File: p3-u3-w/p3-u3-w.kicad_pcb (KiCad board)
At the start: 2 copper layers, 14 x 90 mm, 104 parts, among them J1 SWD_pin, J2 Display, J3 SJ-3524-SMT, J4 473092651, J5 UART, J6 12401826E412A, J7 Bat Conn, J8 CONMHF1-SMD-G-T, SW1 SW_SPST, SW2 SW_SPST, SW3 SW_SPST, SW4 SW_SPST, SW5 SW_SPST, SW6 SW_SPST, SW7 SW_SPST, U1 LSM6DSM, U2 PCM5102A, U3 STM32WB55CEUx, U4 LD39050PU33R, U5 TPS63802DLAR, U6 MCP73831T-2ACI/OT, U7 DLF162500LT-5028A1, X1 NX2016SA-32MHZ-EXS00A-CS06654, Y2 32k768

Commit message: changed some routing
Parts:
- C1, C10, C11, C12, C15, C16, C17, C18, C19, C2, C20, C21, C22, C23, C24, C25, C26, C27, C28, C29, C3, C30, C31, C32, C33, C34, C35, C36, C37, C38, C39, C4, C40, C41, C42, C5, C6, C7, C8, C9: footprint Capacitor_SMD:C_0603_1608Metric -> Capacitor_SMD:C_0402_1005Metric
- C13, C14: footprint Capacitor_SMD:C_0603_1608Metric -> Capacitor_SMD:C_0402_1005Metric; moved to B.Cu
- L1: moved to B.Cu
- R1, R17, R18, R19, R2, R20, R21, R3, R4: footprint Resistor_SMD:R_0603_1608Metric -> Resistor_SMD:R_0402_1005Metric; moved to B.Cu
- R10, R11, R12, R13, R14, R15, R16, R22, R23, R24, R25, R26, R27, R28, R29, R30, R5, R6, R7, R8, R9: footprint Resistor_SMD:R_0603_1608Metric -> Resistor_SMD:R_0402_1005Metric
- moved R3 89.5 mm to (149.0, 78.2)
- moved R4 87.4 mm to (146.6, 78.2), turned to 180 degrees
- moved L1 82.9 mm to (145.5, 108.4), turned to 180 degrees
- moved R2 73.3 mm to (152.8, 56.9)
- moved R20 72.1 mm to (152.7, 70.1)
- moved R21 70.0 mm to (152.7, 79.5)
- moved R19 67.5 mm to (142.5, 56.9), turned to 180 degrees
- moved C13 64.0 mm to (148.7, 83.7), turned to 90 degrees
- moved C14 61.2 mm to (146.1, 83.7), turned to 90 degrees
- moved R1 60.8 mm to (145.8, 79.2)
- moved R18 60.7 mm to (142.5, 70.1), turned to 180 degrees
- moved R17 58.1 mm to (142.6, 79.5), turned to 180 degrees
- moved SW2 26.8 mm to (149.8, 111.7), turned to -90 degrees
- moved C15 11.8 mm to (153.4, 120.2), turned to 0 degrees
- moved U7 9.21 mm to (70.2, 100.3)
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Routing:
- net USB_VBUS: track 49.4 -> 33.2 mm, vias 4 -> 2
- net GND: track 48.0 -> 59.8 mm, vias 27 -> 36
- net +3V3: track 51.4 -> 60.7 mm, vias 10 -> 23
- net /MCU/SWCLK: track 8.54 -> 1.24 mm, vias 0 -> 1
- net Net-(J6-CC1): track 11.1 -> 4.98 mm, vias 2 -> 0
- net /USB_PWR/BAT+: track 18.4 -> 14.3 mm
- net /MCU/SWDIO: track 5.44 -> 1.60 mm, vias 0 -> 1
- net USB_D+: track 8.59 -> 12.0 mm
- net USB_D-: track 13.9 -> 17.0 mm, vias 3 -> 4
- net Net-(U3-PC15): track 4.91 -> 2.88 mm
- net Net-(U5-L1): track 0.00 -> 1.93 mm
- net Net-(U5-L2): track 0.00 -> 1.69 mm
- net Net-(U5-PG): track 4.06 -> 2.39 mm
- net Net-(U5-FB): track 5.43 -> 3.91 mm
- net /MCU/RF1: track 1.02 -> 2.51 mm
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- added copper zone on In1.Cu, net GND
- added copper zone on In4.Cu, net GND
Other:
- copper layers 2 -> 6

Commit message: added in some more routing.
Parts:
- C30, C31: moved to B.Cu
- moved C31 102.2 mm to (153.8, 93.9), turned to 90 degrees
- moved C24 102.1 mm to (149.9, 84.1), turned to 180 degrees
- moved C17 101.9 mm to (149.3, 73.7), turned to 180 degrees
- moved C30 101.7 mm to (153.0, 88.3)
- moved C29 100.8 mm to (146.5, 108.7), turned to 90 degrees
- moved C25 100.3 mm to (149.9, 85.3), turned to 180 degrees
- moved R12 99.8 mm to (152.0, 100.9)
- moved R13 98.8 mm to (151.9, 99.6), turned to 180 degrees
- moved C32 97.6 mm to (153.3, 92.2)
- moved R7 96.5 mm to (148.3, 84.9), turned to 90 degrees
- moved R6 95.2 mm to (146.9, 73.5), turned to 90 degrees
- moved R15 95.1 mm to (151.6, 116.2), turned to 180 degrees
- moved R26 94.6 mm to (151.3, 119.0), turned to -90 degrees
- moved R5 94.0 mm to (145.8, 73.5), turned to 90 degrees
- moved R16 94.0 mm to (153.8, 90.8), turned to -90 degrees
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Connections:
- C1 pad 2: +3V3 -> +3.3V
- C10 pad 2: +3V3 -> +3.3V
- C11 pad 2: +3V3 -> +3.3V
- C12 pad 2: +3V3 -> +3.3V
- C13 pad 2: +3V3 -> +3.3V
- C14 pad 2: +3V3 -> +3.3V
- C18 pad 1: GND -> GNDA
- C18 pad 2: +3.3V -> +3.3VA
- C19 pad 2: GND -> GNDA
- C2 pad 2: +3V3 -> +3.3V
- C20 pad 1: GND -> GNDA
- C20 pad 2: +3.3V -> +3.3VA
- C21 pad 2: GND -> GNDA
- C22 pad 1: GND -> GNDA
- C22 pad 2: +3.3V -> +3.3VA
- C23 pad 1: GND -> GNDA
- C23 pad 2: +3.3V -> +3.3VA
- C24 pad 1: GND -> GNDA
- C25 pad 1: GND -> GNDA
- C26 pad 2: GND -> GNDA
- C27 pad 1: GND -> GNDA
- C27 pad 2: +3.3V -> +3.3VA
- C28 pad 1: GND -> GNDA
- C28 pad 2: +3.3V -> +3.3VA
- C3 pad 2: +3V3 -> +3.3V
- C35 pad 1: +3V3 -> +3.3V
- C36 pad 1: +3V3 -> +3.3V
- C4 pad 2: +3V3 -> +3.3V
- C40 pad 1: +3V3 -> +3.3V
- C5 pad 2: +3V3 -> +3.3V
- C6 pad 2: +3V3 -> +3.3V
- C7 pad 2: +3V3 -> +3.3V
- C8 pad 2: +3V3 -> +3.3V
- C9 pad 2: +3V3 -> +3.3V
- J1 pad 2: +3V3 -> +3.3V
- J2 pad 2: +3V3 -> +3.3V
- J2 pad 3: I2S_SCK -> I2C_SCL
- J3 pad 1: GND -> GNDA
- R1 pad 1: +3V3 -> +3.3V
- R16 pad 1: +3V3 -> +3.3V
- R29 pad 2: +3V3 -> +3.3V
- R3 pad 2: +3V3 -> +3.3V
- R30 pad 2: +3V3 -> +3.3V
- R4 pad 2: +3V3 -> +3.3V
- SW1 pad 2: +3V3 -> +3.3V
- SW2 pad 2: +3V3 -> +3.3V
- SW3 pad 2: +3V3 -> +3.3V
- SW4 pad 2: +3V3 -> +3.3V
- SW5 pad 2: +3V3 -> +3.3V
- SW6 pad 2: +3V3 -> +3.3V
- SW7 pad 2: +3V3 -> +3.3V
- TP2 pad 1: +3V3 -> +3.3V
- U1 pad 13: I2S_SCK -> I2C_SCL
- U1 pad 5: +3V3 -> +3.3V
- U1 pad 8: +3V3 -> +3.3V
- U2 pad 1: +3.3V -> +3.3VA
- U2 pad 17: +3.3V -> +3.3VA
- U2 pad 19: GND -> GNDA
- U2 pad 20: +3.3V -> +3.3VA
- U2 pad 3: GND -> GNDA
- U2 pad 8: +3.3V -> +3.3VA
- U2 pad 9: GND -> GNDA
- U3 pad 1: +3V3 -> +3.3V
- U3 pad 20: +3V3 -> +3.3V
- U3 pad 23: +3V3 -> +3.3V
- U3 pad 34: +3V3 -> +3.3V
- U3 pad 35: +3V3 -> +3.3V
- U3 pad 40: +3V3 -> +3.3V
- U3 pad 48: +3V3 -> +3.3V
- U3 pad 8: +3V3 -> +3.3V
- U4 pad 4: +3V3 -> +3.3V
- U5 pad 6: +3V3 -> +3.3V
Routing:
- net +3.3V: track 0.00 -> 74.3 mm, vias 0 -> 25
- net +3V3: track 60.7 -> 0.00 mm, vias 23 -> 0
- net I2C_SCL: track 1.89 -> 38.4 mm, vias 1 -> 2
- net GND: track 59.8 -> 96.0 mm, vias 36 -> 42
- net I2C_SDA: track 1.24 -> 36.7 mm, vias 1 -> 2
- net BAT_SENSE: track 2.01 -> 28.8 mm
- net SPI_MISO: track 1.87 -> 15.2 mm, vias 1 -> 3
- net SPI_SCK: track 1.30 -> 9.48 mm, vias 1 -> 3
- net Net-(SW2-A): track 2.27 -> 9.69 mm
- net SPI_CS: track 0.66 -> 7.83 mm
- net Net-(U3-NRST): track 2.19 -> 7.22 mm
- net /USB_PWR/BAT+: track 14.3 -> 18.7 mm
- net GNDA: track 0.00 -> 3.38 mm
- net SPI_MOSI: track 1.82 -> 5.11 mm
- net Net-(U2-LDOO): track 0.00 -> 3.26 mm
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- added copper zone on In3.Cu, net +3.3V

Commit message: did some more routing.
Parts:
- C41, C42, J8, L2, U7: moved to B.Cu
- moved C19 104.2 mm to (151.1, 55.5), turned to -90 degrees
- moved C23 103.5 mm to (151.1, 72.3), turned to 180 degrees
- moved C22 103.3 mm to (151.1, 73.3), turned to 180 degrees
- moved C27 101.5 mm to (152.2, 84.0), turned to 90 degrees
- moved C28 100.2 mm to (151.6, 81.3), turned to -90 degrees
- moved C21 99.0 mm to (143.2, 47.6), turned to 180 degrees
- moved C18 97.8 mm to (145.3, 74.6)
- moved C20 97.5 mm to (145.3, 73.6)
- moved C26 96.6 mm to (148.3, 72.1), turned to 90 degrees
- moved C41 48.9 mm to (153.2, 101.3), turned to 90 degrees
- moved L2 48.7 mm to (152.3, 103.8), turned to -90 degrees
- moved C42 46.6 mm to (152.7, 106.3), turned to -90 degrees
- moved U7 39.8 mm to (150.5, 104.6), turned to 180 degrees
- moved J8 30.2 mm to (149.5, 107.7), turned to 180 degrees
- moved R5 10.5 mm to (147.6, 63.2)
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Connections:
- U3 pad 28: BTN_VOL- -> BTN_PREV
- U3 pad 29: BTN_VOL+ -> BTN_NEXT
- U3 pad 43: BTN_PREV -> BTN_VOL-
- U3 pad 44: BTN_NEXT -> BTN_VOL+
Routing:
- net BTN_PLY: track 2.41 -> 49.6 mm, vias 1 -> 2
- net BTN_MENU: track 2.56 -> 39.2 mm, vias 1 -> 3
- net USB_D-: track 17.0 -> 51.5 mm, vias 4 -> 5
- net USB_D+: track 12.0 -> 43.6 mm, vias 2 -> 3
- net BTN_NEXT: track 1.50 -> 28.8 mm, vias 1 -> 2
- net BTN_VOL+: track 1.16 -> 28.1 mm, vias 1 -> 2
- net GND: track 96.0 -> 119.2 mm, vias 42 -> 45
- net Net-(SW2-A): track 9.69 -> 29.4 mm, vias 1 -> 2
- net Net-(C21-Pad1): track 0.00 -> 19.6 mm, vias 0 -> 1
- net BTN_PREV: track 2.00 -> 20.6 mm, vias 1 -> 2
- net +3.3V: track 74.3 -> 90.3 mm, vias 25 -> 26
- net I2S_SCK: track 1.70 -> 17.6 mm
- net I2S_FS: track 1.35 -> 17.2 mm, vias 1 -> 3
- net Net-(U2-OUTR): track 0.00 -> 13.7 mm
- net IMU_SAO: track 1.13 -> 14.8 mm, vias 1 -> 2
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
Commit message: finished routing need to pass drc
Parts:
- moved C27 2.92 mm to (151.1, 86.7)
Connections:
- C18 pad 1: GNDA -> GND
- C18 pad 2: +3.3VA -> +3.3V
- C19 pad 2: GNDA -> GND
- C20 pad 1: GNDA -> GND
- C20 pad 2: +3.3VA -> +3.3V
- C21 pad 2: GNDA -> GND
- C22 pad 1: GNDA -> GND
- C22 pad 2: +3.3VA -> +3.3V
- C23 pad 1: GNDA -> GND
- C23 pad 2: +3.3VA -> +3.3V
- C24 pad 1: GNDA -> GND
- C25 pad 1: GNDA -> GND
- C26 pad 2: GNDA -> GND
- C27 pad 1: GNDA -> GND
- C27 pad 2: +3.3VA -> +3.3V
- C28 pad 1: GNDA -> GND
- C28 pad 2: +3.3VA -> +3.3V
- J3 pad 1: GNDA -> GND
- U2 pad 1: +3.3VA -> +3.3V
- U2 pad 17: +3.3VA -> +3.3V
- U2 pad 19: GNDA -> GND
- U2 pad 20: +3.3VA -> +3.3V
- U2 pad 3: GNDA -> GND
- U2 pad 8: +3.3VA -> +3.3V
- U2 pad 9: GNDA -> GND
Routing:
- net GND: track 119.2 -> 165.3 mm, vias 45 -> 58
- net +3.3V: track 90.3 -> 123.8 mm, vias 26 -> 31
- net IMU_INT2: track 5.43 -> 18.7 mm, vias 1 -> 3
- net IMU_INT1: track 3.63 -> 14.5 mm, vias 2 -> 3
- net +3.3VA: track 10.3 -> 0.00 mm
- net GNDA: track 5.39 -> 0.00 mm
- net BTN_VOL-: track 14.8 -> 16.9 mm
- net BTN_MENU: track 39.2 -> 41.3 mm, vias 3 -> 4
- net BTN_PREV: track 20.6 -> 22.5 mm
- net BTN_VOL+: track 28.1 -> 30.0 mm
- net BTN_PLY: track 49.6 -> 51.5 mm
- net BTN_NEXT: track 28.8 -> 30.7 mm
- net IMU_SAO: track 14.8 -> 16.7 mm
- added copper zone on In2.Cu, net +3.3V
- added copper zone on B.Cu, net GND
- added copper zone on F.Cu, net GND
- added copper zone on In2.Cu, net GND

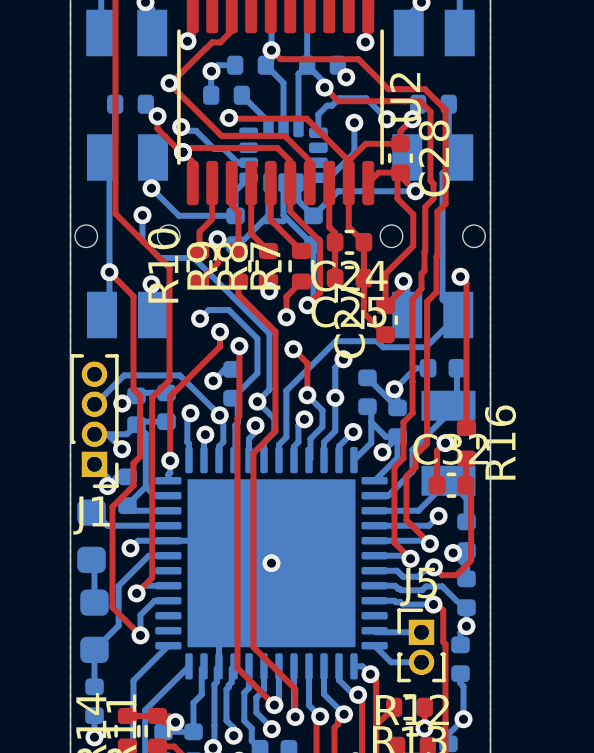
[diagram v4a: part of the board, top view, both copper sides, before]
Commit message: did drc mostly finished drc, need to remove silkscreen designators aswell.
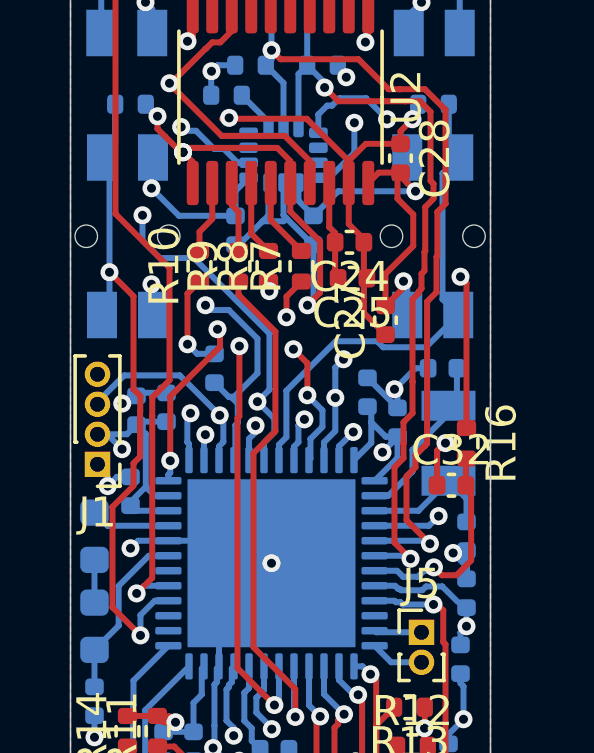
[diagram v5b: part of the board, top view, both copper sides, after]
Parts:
- moved C12 0.79 mm to (145.4, 88.3)
- moved C10 0.10 mm to (142.6, 92.4)
- moved C25 0.10 mm to (150.0, 85.3)
- moved J1 0.10 mm to (141.5, 91.5)
- moved L4 0.10 mm to (141.4, 93.9)
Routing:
- net +3.3V: track 123.8 -> 124.5 mm
- net GND: track 165.3 -> 165.4 mm, vias 58 -> 57
